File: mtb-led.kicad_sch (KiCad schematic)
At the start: 0 parts

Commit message: Sch: add basic information.
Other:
- company: (none) -> Model Railroader Club Brno I – KMŽ Brno I – https://kmz-brno.cz/
- title: (none) -> MTB-LED - MTBbus LED driver - root schematic
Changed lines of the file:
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@@
 	(generator_version "9.0")
 	(paper "A4")
+	(title_block
+		(title "MTB-LED - MTBbus LED driver - root schematic")
+		(date "2026-05-10")
+		(rev "1.0")
+		(company "Model Railroader Club Brno I – KMŽ Brno I – https://kmz-brno.cz/")
+		(comment 1 "Jan Malina")
+		(comment 2 "https://github.com/kmzbrnoI/mtb-led-hw https://mtb.kmz-brno.cz/")
+		(comment 3 "https://creativecommons.org/licenses/by-sa/4.0/")
+		(comment 4 "Released under the Creative Commons Attribution-ShareAlike 4.0 License")
+	)
 	(sheet_instances
 		(path "/"

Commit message: Sch: add basic parts, wire power supply.
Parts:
- added C1, C2: 100n, symbol Device:C
- added C3: 22u/25V, symbol Device:C
- added C4: 22u, symbol Device:C
- added C5, C6: C, symbol Device:C
- added D1: 1N5819, symbol Device:D_Schottky
- added D2: BZX84C18, Package_TO_SOT_SMD:SOT-23, symbol Diode:BZX84Cxx
- added D3: BT148, symbol Device:Q_SCR_KAG
- added D4: SM712_SOT23, Package_TO_SOT_SMD:SOT-23, symbol Diode:SM712_SOT23
- added D5: SS34, Diode_SMD:D_SMA_Handsoldering, symbol Diode:SS34
- added F1: 200mA, symbol Device:Polyfuse
- added F2: 1A, symbol Device:Polyfuse
- added J1, J2: ~, Connector_Phoenix_MSTB:PhoenixContact_MSTBA_2,5_4-G_1x04_P5.00mm_Horizontal, symbol Connector:Screw_Terminal_01x04
- added J3, J4, J5, J6: ~, Connector_Phoenix_MC:PhoenixContact_MC_1,5_10-G-3.5_1x10_P3.50mm_Horizontal, symbol Connector:Screw_Terminal_01x10
- added J7: AVR-ISP-6, symbol Connector:AVR-ISP-6
- added R1: 2k2, symbol Device:R
- added SW1: SW_Push, symbol Switch:SW_Push
- added U1: ATmega328PB-A, Package_QFP:TQFP-32_7x7mm_P0.8mm, symbol MCU_Microchip_ATmega:ATmega328PB-A
- added U2: 78M05, Package_TO_SOT_SMD:TO-252-2, symbol Regulator_Linear:KA78M05_TO252
- added U3, U4: TLC5940PWP, Package_SO:HTSSOP-28-1EP_4.4x9.7mm_P0.65mm_EP3.4x9.5mm_Mask2.4x6.17mm_ThermalVias, symbol Driver_LED:TLC5940PWP
- added U5: MAX487E, Package_SO:SOIC-8_3.9x4.9mm_P1.27mm, symbol Interface_UART:MAX487E
- added Y1: Crystal, symbol Device:Crystal
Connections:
- new net: C3.1, D1.1 (K), D2.3 (K), D3.2 (A), U2.1 (VI)
- new net: C2.1, D2.1 (A), D3.3 (G), R1.1
- new net: D5.2 (A), F2.2
- new net: C1.1, D1.2 (A), F1.2
- new net: U1.21 (GND), U1.5 (GND)
- new net +12V: D5.1 (K)
- new net +12V-IN: F1.1, F2.1, J1.1 (Pin_1), J2.4 (Pin_4)
- new net +5V: C4.1, U2.3 (VO)
- new net BUS+: J1.3 (Pin_3), J2.2 (Pin_2)
- new net BUS-: J1.4 (Pin_4), J2.1 (Pin_1)
- new net GND: C1.2, C2.2, C3.2, C4.2, D3.1 (K), J1.2 (Pin_2), J2.3 (Pin_3), R1.2, U2.2 (GND)

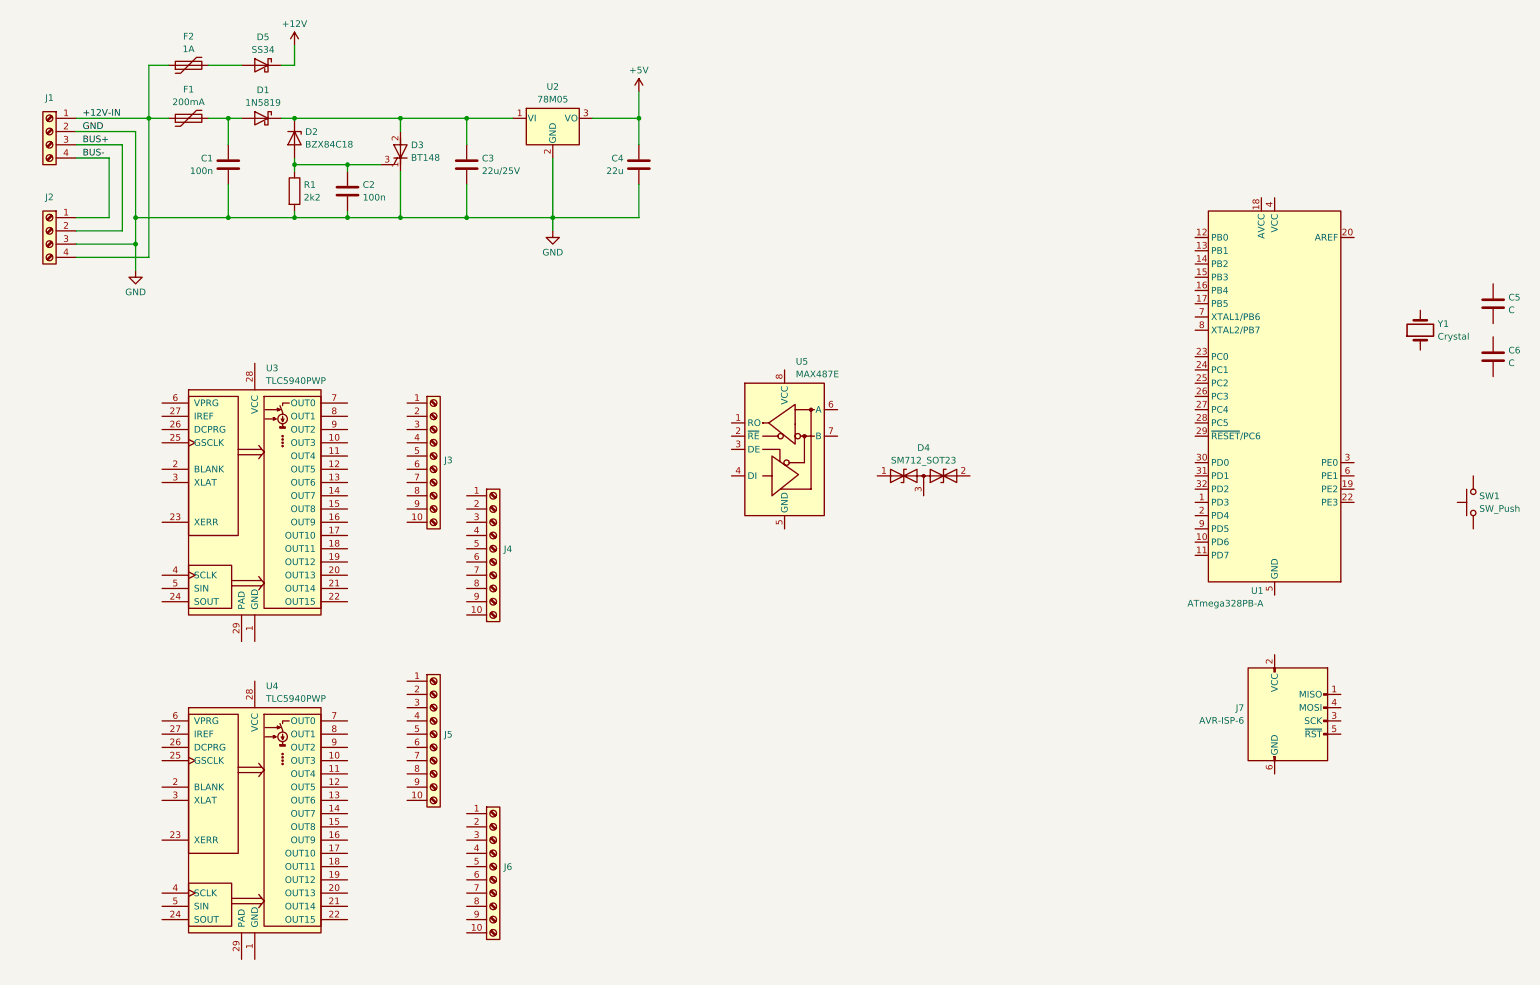
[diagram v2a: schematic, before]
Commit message: Sch: wire outputs.
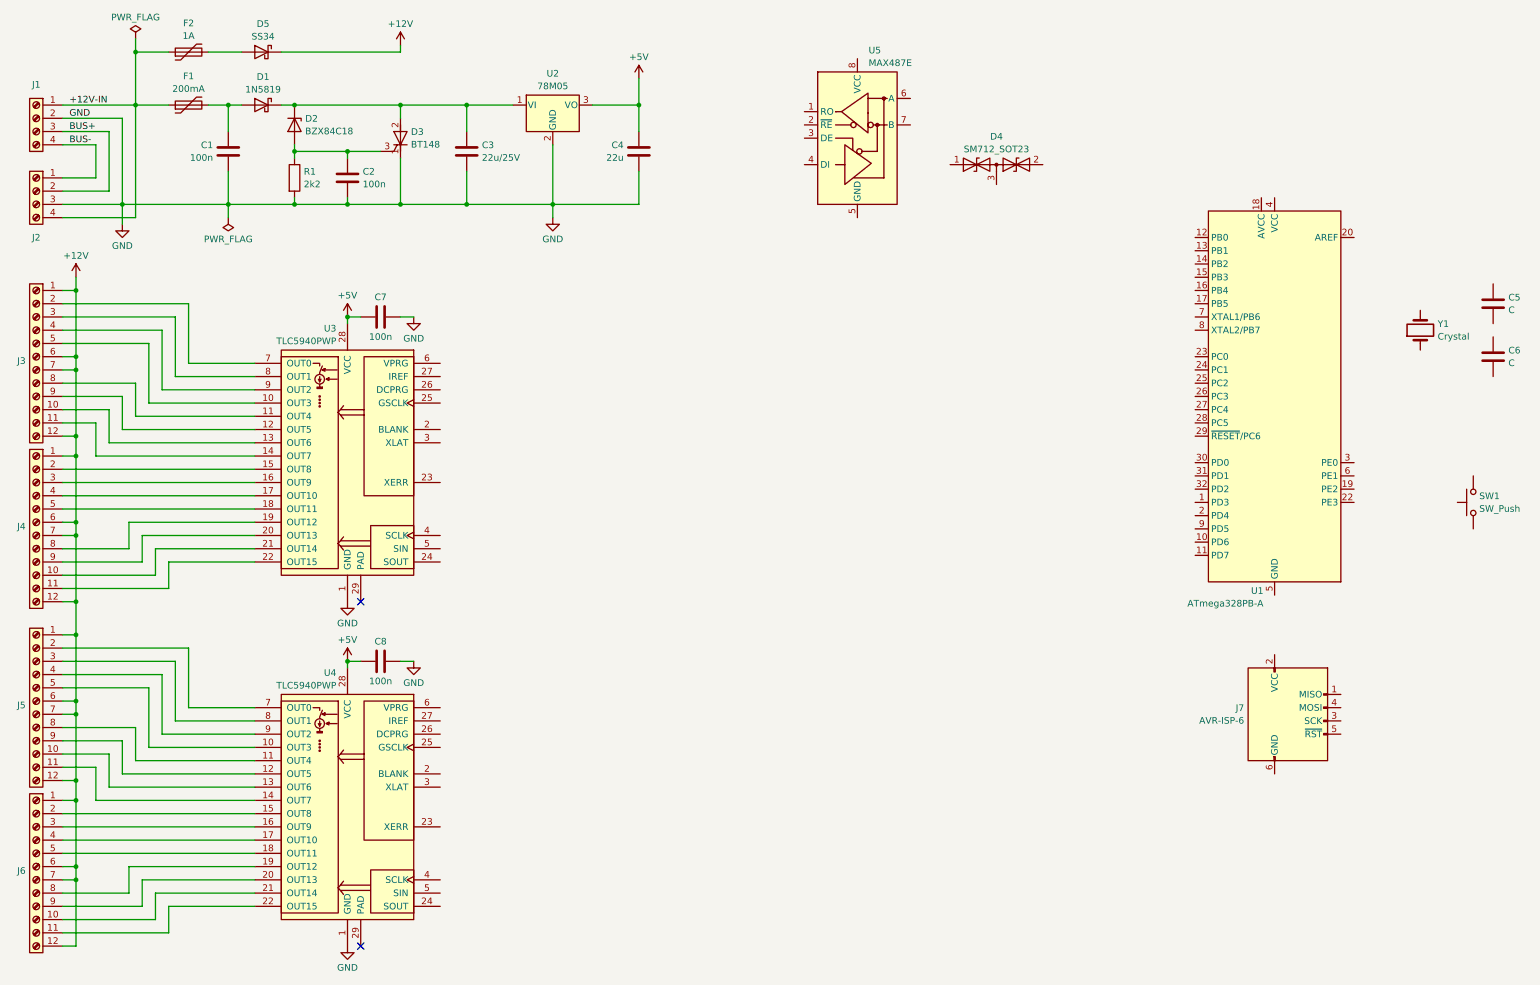
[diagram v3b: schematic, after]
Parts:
- added C7, C8: 100n, symbol Device:C
- J3, J4, J5, J6: footprint Connector_Phoenix_MC:PhoenixContact_MC_1,5_10-G-3.5_1x10_P3.50mm_Horizontal -> Connector_Phoenix_MC:PhoenixContact_MC_1,5_12-G-3.5_1x12_P3.50mm_Horizontal; symbol Connector:Screw_Terminal_01x10 -> Connector:Screw_Terminal_01x12
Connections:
- net +12V: now also J3.1 (Pin_1), J3.12 (Pin_12), J3.6 (Pin_6), J3.7 (Pin_7), J4.1 (Pin_1), J4.12 (Pin_12), J4.6 (Pin_6), J4.7 (Pin_7), J5.1 (Pin_1), J5.12 (Pin_12), J5.6 (Pin_6), J5.7 (Pin_7), J6.1 (Pin_1), J6.12 (Pin_12), J6.6 (Pin_6), J6.7 (Pin_7)
- net +5V: now also U3.28 (VCC), U4.28 (VCC), C7.1, C8.1
- net GND: now also U3.1 (GND), U4.1 (GND), C7.2, C8.2
- net at J5.10 (Pin_10): now also U4.13 (OUT6)
- net at J5.2 (Pin_2): now also U4.7 (OUT0)
- net at J5.3 (Pin_3): now also U4.8 (OUT1)
- net at J5.4 (Pin_4): now also U4.9 (OUT2)
- net at J5.5 (Pin_5): now also U4.10 (OUT3)
- net at J5.8 (Pin_8): now also U4.11 (OUT4)
- net at J5.9 (Pin_9): now also U4.12 (OUT5)
- net at J6.10 (Pin_10): now also U4.21 (OUT14)
- net at J6.2 (Pin_2): now also U4.15 (OUT8)
- net at J6.3 (Pin_3): now also U4.16 (OUT9)
- net at J6.4 (Pin_4): now also U4.17 (OUT10)
- net at J6.5 (Pin_5): now also U4.18 (OUT11)
- net at J6.8 (Pin_8): now also U4.19 (OUT12)
- net at J6.9 (Pin_9): now also U4.20 (OUT13)
- net at J3.10 (Pin_10): now also U3.13 (OUT6)
- net at J3.2 (Pin_2): now also U3.7 (OUT0)
- net at J3.3 (Pin_3): now also U3.8 (OUT1)
- net at J3.4 (Pin_4): now also U3.9 (OUT2)
- net at J3.5 (Pin_5): now also U3.10 (OUT3)
- net at J3.8 (Pin_8): now also U3.11 (OUT4)
- net at J3.9 (Pin_9): now also U3.12 (OUT5)
- net at J4.10 (Pin_10): now also U3.21 (OUT14)
- net at J4.2 (Pin_2): now also U3.15 (OUT8)
- net at J4.3 (Pin_3): now also U3.16 (OUT9)
- net at J4.4 (Pin_4): now also U3.17 (OUT10)
- net at J4.5 (Pin_5): now also U3.18 (OUT11)
- net at J4.8 (Pin_8): now also U3.19 (OUT12)
- net at J4.9 (Pin_9): now also U3.20 (OUT13)
- net at U3.14 (OUT7): now also J3.11 (Pin_11)
- net at U3.22 (OUT15): now also J4.11 (Pin_11)
- net at U4.14 (OUT7): now also J5.11 (Pin_11)
- net at U4.22 (OUT15): now also J6.11 (Pin_11)
- no-connect marks 0 -> 2
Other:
- moved on the sheet: C1, C2, C3, C4, D1, D2, D3, D4, D5, F1, F2, J1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

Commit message: Sch: add MTBbus interface.
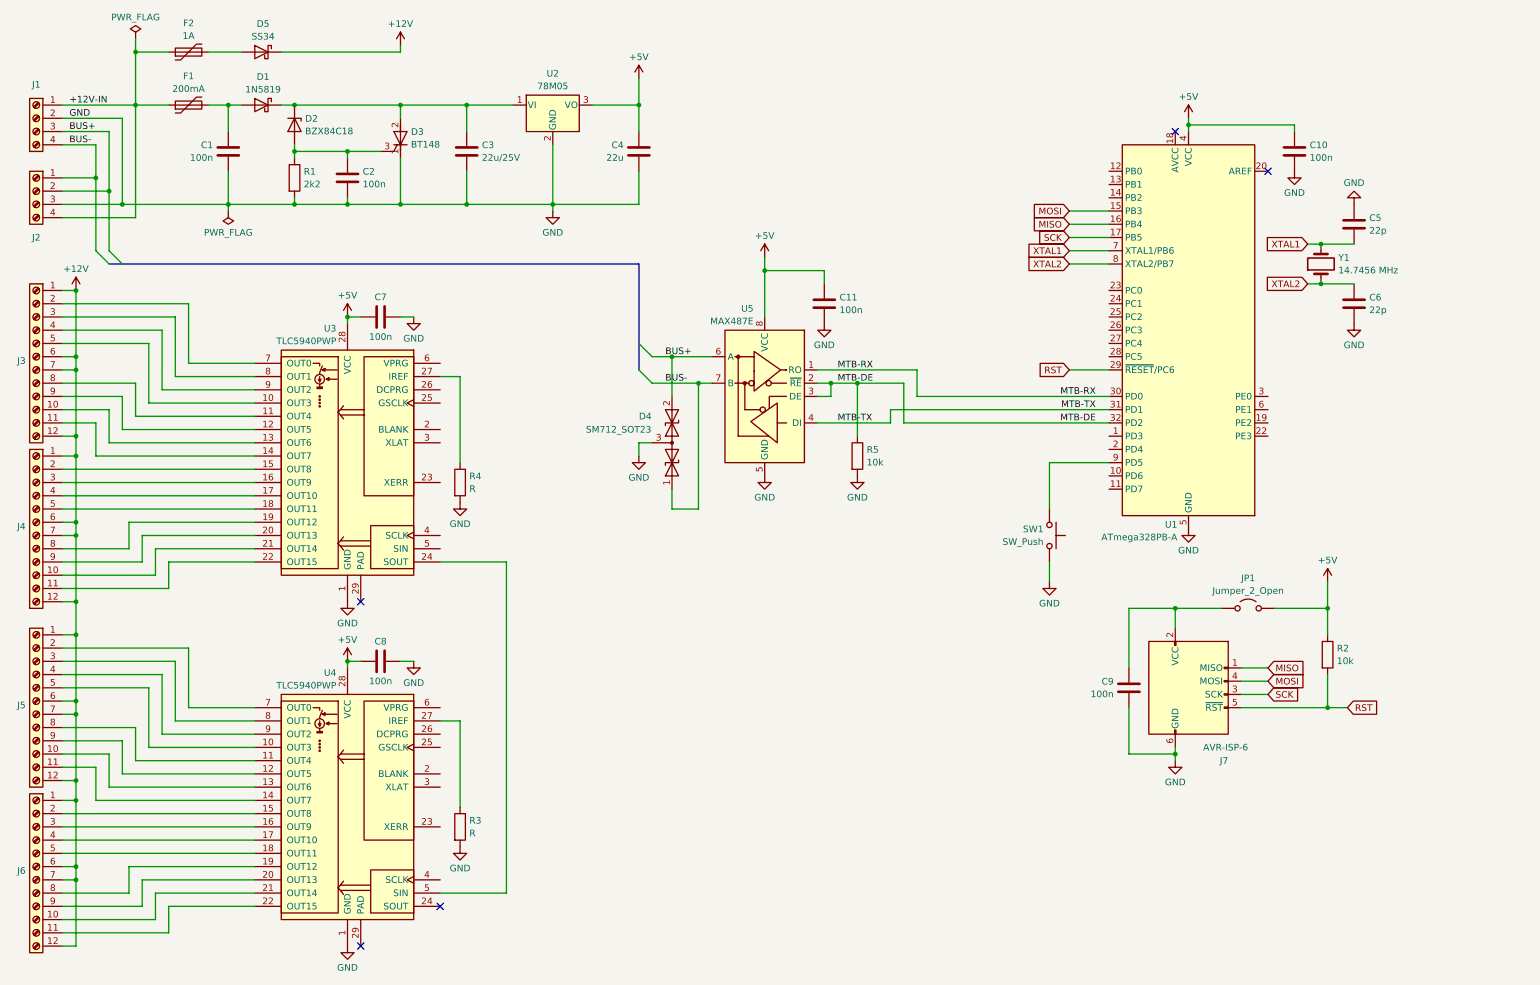
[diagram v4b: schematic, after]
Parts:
- added C10, C11, C9: 100n, symbol Device:C
- added JP1: Jumper_2_Open, symbol Jumper:Jumper_2_Open
- added R2, R5: 10k, symbol Device:R
- added R3, R4: R, symbol Device:R
- C5, C6: value C -> 22p
- Y1: value Crystal -> 14.7456 MHz
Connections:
- net +5V: now also U1.4 (VCC), U5.8 (VCC), C10.1, C11.1, JP1.2 (B), R2.1
- net BUS+: now also D4.2 (A2), U5.6 (A)
- net BUS-: now also D4.1 (A1), U5.7 (B)
- net GND: now also C5.1, C6.2, D4.3 (common), J7.6 (GND), SW1.1, U1.21 (GND), U1.5 (GND), U5.5 (GND), C10.2, C11.2, C9.2, R3.2, R4.2, R5.2
- net XTAL2: now reaches C6.1
- net XTAL2: now also U1.8 (XTAL2/PB7), Y1.1
- net XTAL1: now reaches Y1.2
- net XTAL1: now also C5.2, U1.7 (XTAL1/PB6)
- net MOSI: now reaches U1.15 (PB3)
- net MOSI: now also J7.4 (MOSI)
- net MISO: now reaches U1.16 (PB4)
- net MISO: now also J7.1 (MISO)
- net SCK: now reaches U1.17 (PB5)
- net SCK: now also J7.3 (SCK)
- net RST: now reaches U1.29 (~{RESET}/PC6)
- net RST: now also J7.5 (~{RST}), R2.2
- net MTB-RX: now reaches U1.30 (PD0)
- net MTB-RX: now also U5.1 (RO)
- net MTB-TX: now reaches U1.31 (PD1)
- net MTB-TX: now also U5.4 (DI)
- net MTB-DE: now reaches U1.32 (PD2)
- net MTB-DE: now also U5.2 (~{RE}), U5.3 (DE), R5.1
- net at U1.9 (PD5): now also SW1.2
- net at U3.24 (SOUT): now also U4.5 (SIN)
- net at U3.27 (IREF): now also R4.1
- net at J7.2 (VCC): now also C9.1, JP1.1 (A)
- net at U4.27 (IREF): now also R3.1
- no-connect marks 2 -> 5
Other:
- moved on the sheet: C5, C6, D4, J7, SW1, U1, U5, Y1

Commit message: Sch: connect TLS5940 and MCU.
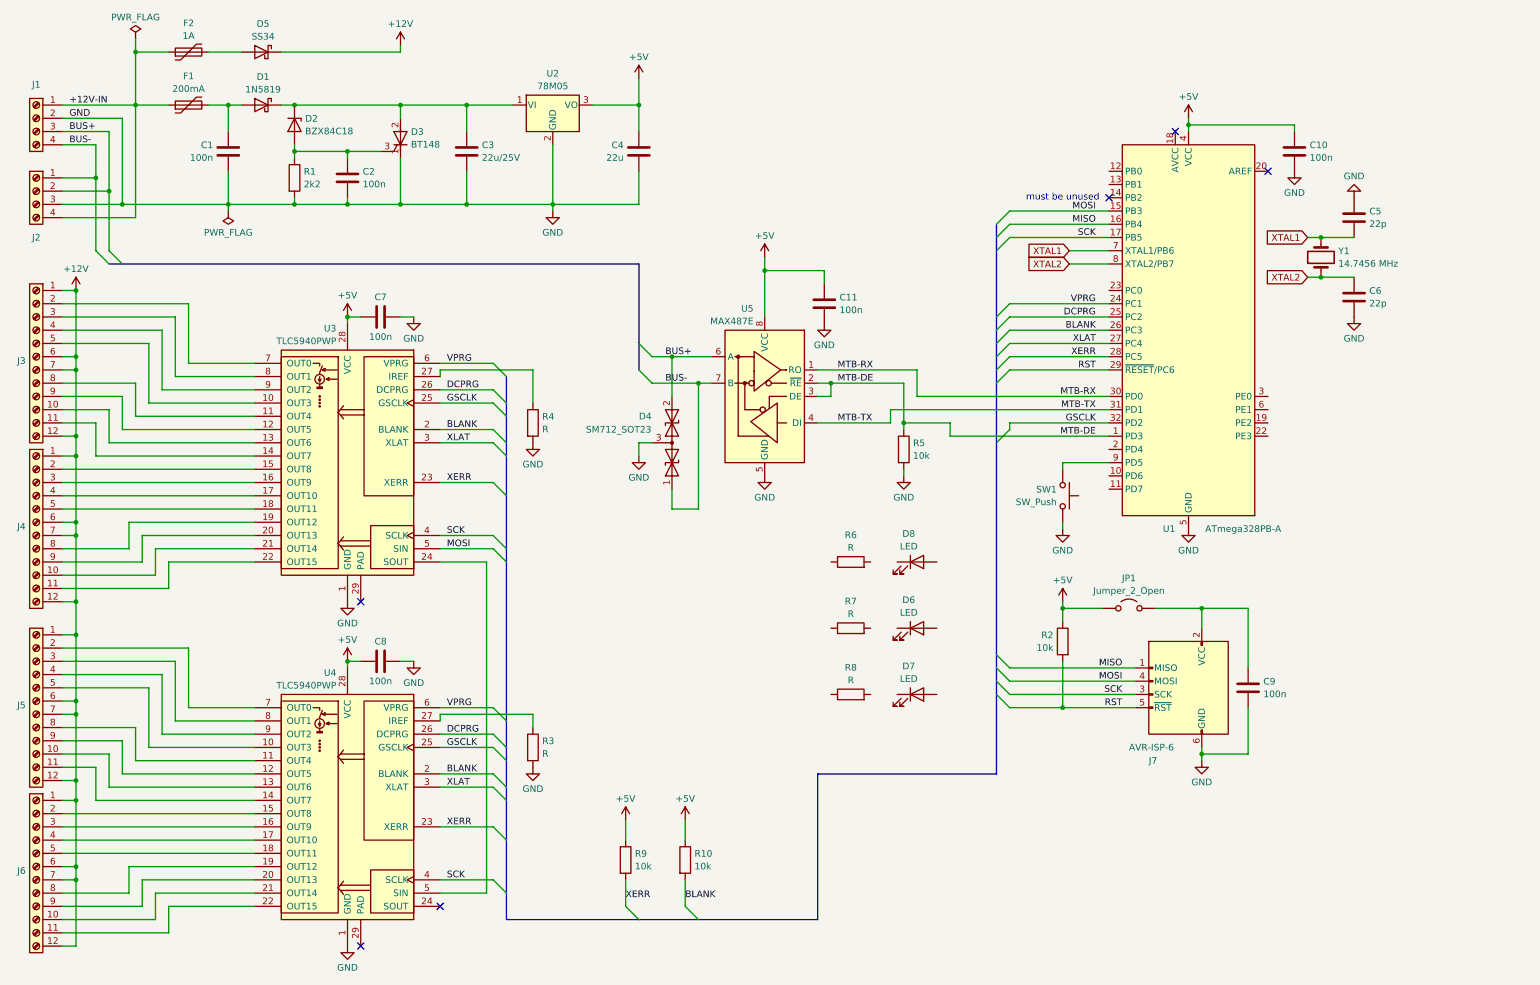
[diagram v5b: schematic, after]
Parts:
- added D6, D7, D8: LED, symbol Device:LED
- added R10, R9: 10k, symbol Device:R
- added R6, R7, R8: R, symbol Device:R
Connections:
- net +5V: now also R10.1, R9.1
- net MOSI: now also U3.5 (SIN)
- net MTB-DE: now also U1.1 (PD3); no longer U1.32 (PD2)
- net SCK: now also U3.4 (SCLK), U4.4 (SCLK)
- net VPRG: now reaches U1.24 (PC1)
- net VPRG: now also U3.6 (VPRG), U4.6 (VPRG)
- net DCPRG: now reaches U1.25 (PC2)
- net DCPRG: now also U3.26 (DCPRG), U4.26 (DCPRG)
- net BLANK: now reaches U1.26 (PC3)
- net BLANK: now also U3.2 (BLANK), U4.2 (BLANK), R10.2
- net XLAT: now reaches U1.27 (PC4)
- net XLAT: now also U3.3 (XLAT), U4.3 (XLAT)
- net XERR: now reaches U1.28 (PC5)
- net XERR: now also U3.23 (XERR), U4.23 (XERR), R9.2
- net GSCLK: now reaches U3.25 (GSCLK)
- net GSCLK: now also U1.32 (PD2), U4.25 (GSCLK)
- no-connect marks 5 -> 6
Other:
- note added: "must be unused"
- moved on the sheet: C5, C6, C9, J7, JP1, R2, R3, R4, R5, SW1, Y1
